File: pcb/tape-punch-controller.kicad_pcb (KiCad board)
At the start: 2 copper layers, 70 x 88 mm, 148 parts, among them J1 Conn_01x06, J2 Conn_01x09, J3 USB_B, J4 Conn_01x16, J5 Conn_01x06, J6 Conn_01x02, J7 Conn_02x03_Odd_Even, J8 Conn_01x04, Q1 IRLML0060, Q10 IRLML0060, Q2 IRLML0060, Q3 IRLML0060, Q4 IRLML0060, Q5 IRLML0060, Q6 IRLML0060, Q7 IRLML0060, Q8 IRLML0060, Q9 IRLML0060, SW1 SW_Push, U1 ATXMEGA192C3-AU, U2 LM321, U3 USBLC6-2SC6, U4 TSR_1-2433, U5 TSR_1-24150

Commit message: pcb: rearrange labels on back silkscreen
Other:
- board text added: "2018/01 Kier Davis me@kierdavis.com"
- board text added: "TP MISC"
- board text added: "TP SOLENOIDS"
- board text removed: "Kier Davis 2018/01 me@kierdavis.com"
- board text removed: "TAPE PNCH"
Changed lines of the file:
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@@
     (links 278)
     (no_connects 0)
-    (area 91.949999 19.949999 162.050001 108.050001)
+    (area 89.371428 18 164.628573 110.000001)
     (thickness 1.6)
-    (drawings 65)
+    (drawings 74)
     (tracks 709)
     (zones 0)
@@
     (pad_to_mask_clearance 0)
     (aux_axis_origin 0 0)
-    (visible_elements FFFEFE7F)
+    (visible_elements FFFFFE7F)
     (pcbplotparams
-      (layerselection 0x00030_80000001)
+      (layerselection 0x010f0_80000001)
       (usegerberextensions false)
       (excludeedgelayer true)
@@
       (outputformat 1)
       (mirror false)
-      (drillshape 1)
+      (drillshape 0)
       (scaleselection 1)
-      (outputdirectory ""))
+      (outputdirectory out/))
   )
   (net 0 "")
@@
       (net 4 /Microcontroller/USB_SHIELD))
   )
+  (gr_line (start 105.41 52.705) (end 106.68 53.975) (angle 90) (layer B.SilkS) (width 0.2))
+  (gr_line (start 106.68 51.435) (end 105.41 52.705) (angle 90) (layer B.SilkS) (width 0.2))
+  (gr_line (start 105.41 52.705) (end 111.76 52.705) (angle 90) (layer B.SilkS) (width 0.2))
+  (gr_line (start 107.95 78.74) (end 111.76 78.74) (angle 90) (layer B.SilkS) (width 0.2))
+  (gr_line (start 106.68 80.01) (end 107.95 78.74) (angle 90) (layer B.SilkS) (width 0.2))
+  (gr_line (start 106.68 80.01) (end 107.95 80.01) (angle 90) (layer B.SilkS) (width 0.2))
+  (gr_line (start 106.68 78.74) (end 106.68 80.01) (angle 90) (layer B.SilkS) (width 0.2))
+  (gr_line (start 111.76 65.405) (end 115.57 65.405) (angle 90) (layer B.SilkS) (width 0.2))
+  (gr_text "TP MISC" (at 113.665 79.375 270) (layer B.SilkS)
+    (effects (font (size 2 2) (thickness 0.3)) (justify left mirror))
+  )
+  (gr_text "TP SOLENOIDS" (at 113.665 41.91 270) (layer B.SilkS)
+    (effects (font (size 2 2) (thickness 0.3)) (justify right mirror))
+  )
   (gr_arc (start 156 26) (end 156 20) (angle 90) (layer Edge.Cuts) (width 0.1))
   (gr_arc (start 98 26) (end 92 26) (angle 90) (layer Edge.Cuts) (width 0.1))
@@
     (effects (font (size 1.5 1.5) (thickness 0.375)) (justify left mirror))
   )
-  (gr_text "Kier Davis   2018/01\nme@kierdavis.com" (at 114.935 77.597 270) (layer B.SilkS)
+  (gr_text "2018/01\nKier Davis\nme@kierdavis.com" (at 125.095 27.305 180) (layer B.SilkS)
     (effects (font (size 2 2) (thickness 0.3)) (justify left mirror))
   )
@@
     (effects (font (size 2 2) (thickness 0.4)) (justify mirror))
   )
-  (gr_text "TAPE PNCH" (at 94.615 88.265 270) (layer B.SilkS)
-    (effects (font (size 2 2) (thickness 0.4)) (justify mirror))
-  )

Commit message: pcb: make format of date label clearer
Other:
- board text added: "Jan 2018 Kier Davis me@kierdavis.com"
- board text removed: "2018/01 Kier Davis me@kierdavis.com"
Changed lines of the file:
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@@
     (effects (font (size 1.5 1.5) (thickness 0.375)) (justify left mirror))
   )
-  (gr_text "2018/01\nKier Davis\nme@kierdavis.com" (at 125.095 27.305 180) (layer B.SilkS)
+  (gr_text "Jan 2018\nKier Davis\nme@kierdavis.com" (at 125.095 27.305 180) (layer B.SilkS)
     (effects (font (size 2 2) (thickness 0.3)) (justify left mirror))
   )

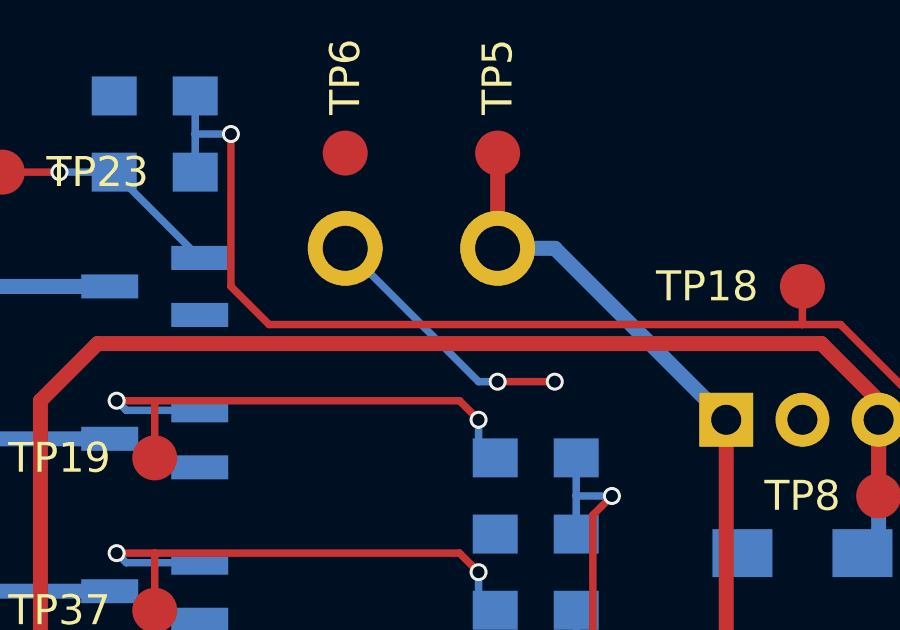
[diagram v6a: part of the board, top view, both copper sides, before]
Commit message: pcb: increase length of isolation gap between high-current and low-current ground plane regions
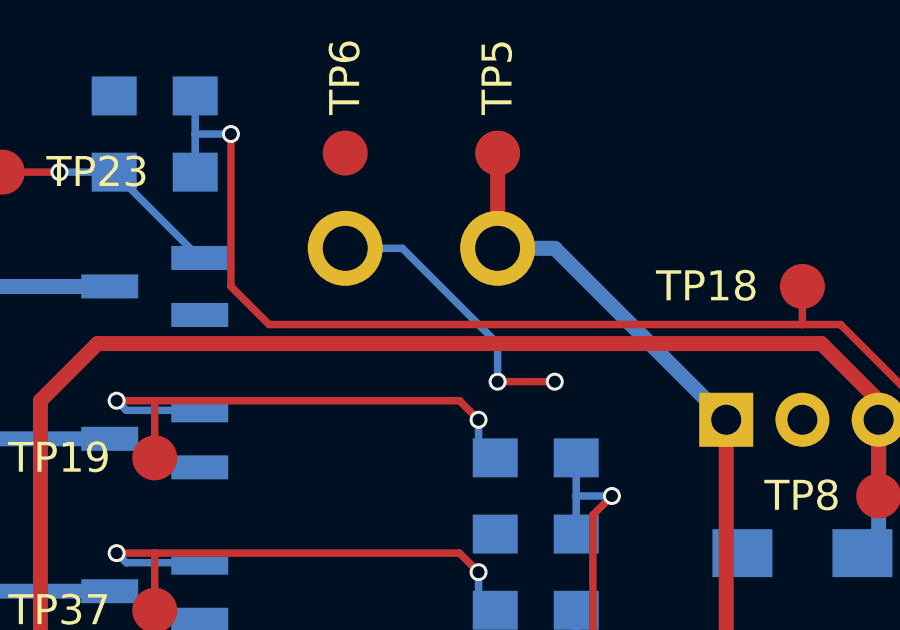
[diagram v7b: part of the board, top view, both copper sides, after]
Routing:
- net GND: track 28.4 -> 29.2 mm
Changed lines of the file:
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@@
     (thickness 1.6)
     (drawings 74)
-    (tracks 709)
+    (tracks 710)
     (zones 0)
     (modules 148)
@@
   (segment (start 146.05 86.36) (end 146.05 89.555) (width 0.5) (layer B.Cu) (net 1))
   (segment (start 145.535 85.845) (end 146.05 86.36) (width 0.5) (layer B.Cu) (net 1))
-  (segment (start 114.935 33.655) (end 119.38 38.1) (width 0.25) (layer B.Cu) (net 2))
   (via (at 121.92 38.1) (size 0.6) (drill 0.4) (layers F.Cu B.Cu) (net 2))
-  (segment (start 120.015 38.1) (end 121.92 38.1) (width 0.25) (layer F.Cu) (net 2))
+  (segment (start 116.84 33.655) (end 120.015 36.83) (width 0.25) (layer B.Cu) (net 2))
+  (segment (start 120.015 36.83) (end 120.015 38.1) (width 0.25) (layer B.Cu) (net 2))
   (via (at 120.015 38.1) (size 0.6) (drill 0.4) (layers F.Cu B.Cu) (net 2))
-  (segment (start 119.38 38.1) (end 120.015 38.1) (width 0.25) (layer B.Cu) (net 2))
+  (segment (start 121.92 38.1) (end 120.015 38.1) (width 0.25) (layer F.Cu) (net 2))
+  (segment (start 116.84 33.655) (end 114.935 33.655) (width 0.25) (layer B.Cu) (net 2))
   (segment (start 133.75 99.6) (end 137.16 96.19) (width 0.25) (layer F.Cu) (net 2))
   (via (at 137.16 93.98) (size 0.6) (drill 0.4) (layers F.Cu B.Cu) (net 2))
@@
     (polygon
       (pts
-        (xy 116.84 36.83) (xy 116.84 78.74) (xy 107.95 78.74) (xy 107.95 34.29) (xy 111.125 34.29)
+        (xy 116.84 34.925) (xy 116.84 78.74) (xy 107.95 78.74) (xy 107.95 34.29) (xy 111.125 34.29)
         (xy 111.125 33.655) (xy 110.49 33.655) (xy 107.315 33.655) (xy 107.315 79.375) (xy 117.475 79.375)
-        (xy 117.475 36.83)
+        (xy 117.475 34.925)
       )
     )
